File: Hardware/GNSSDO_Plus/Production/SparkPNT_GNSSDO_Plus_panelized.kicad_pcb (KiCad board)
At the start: 4 copper layers, 165.6 x 125.5 mm, 478 parts, among them J1 SMA_Edge, J10 SMA_Edge, J2 USB_C_Receptacle, J3 SMA_Edge, J4 USB_C_Receptacle, J5 MagJack_PoE, J6 microSD, J7 Qwiic_Vertical, J8 SMA_Edge, J9 Screw_Cage_3.5mm-10, Q1 MBT3904DW1, Q2 DMG2305UX, Q3 DMG2305UX, Q4 DMG2305UX, Q5 DMG2305UX, Q6 DMG2305UX, Q7 DMG2305UX, Q8 DMG2305UX, Q9 DMG2305UX, SW1 PTH_RA_h7.5mm, SW2 PTH_RA_h7.5mm, SW3 PTH_RA_h7.5mm, SW4 DPDT_Slide_SMD_7.2x3.5mm, U1 ESP32-WROVER-IE-N16R8, U10 74LVC2T45DC, U11 AP7361C-3.3V, U12 74LVC2T45DC, U13 STP3593LF, U14 74LVC2T45DC, U15 SN74LVC1G175DCK, U16 JPS-3-1+, U17 LMV7219M5, U18 MS8607-02BA, U19 PCA9306, U2 mosaic-T, U20 LMV7219M5, U23 LMV7219M5, U24 LMV7219M5, U25 AP2112K-3.3, U26 LTC4418, U27 LTC4418, U3 CH340C, U4 KSZ8041NL/I, U5 AP7361C-3.3V, U6 REC15E-2405SZ, U7 DP5305, U8 74LVC2T45DC, U9 74LVC2T45DC

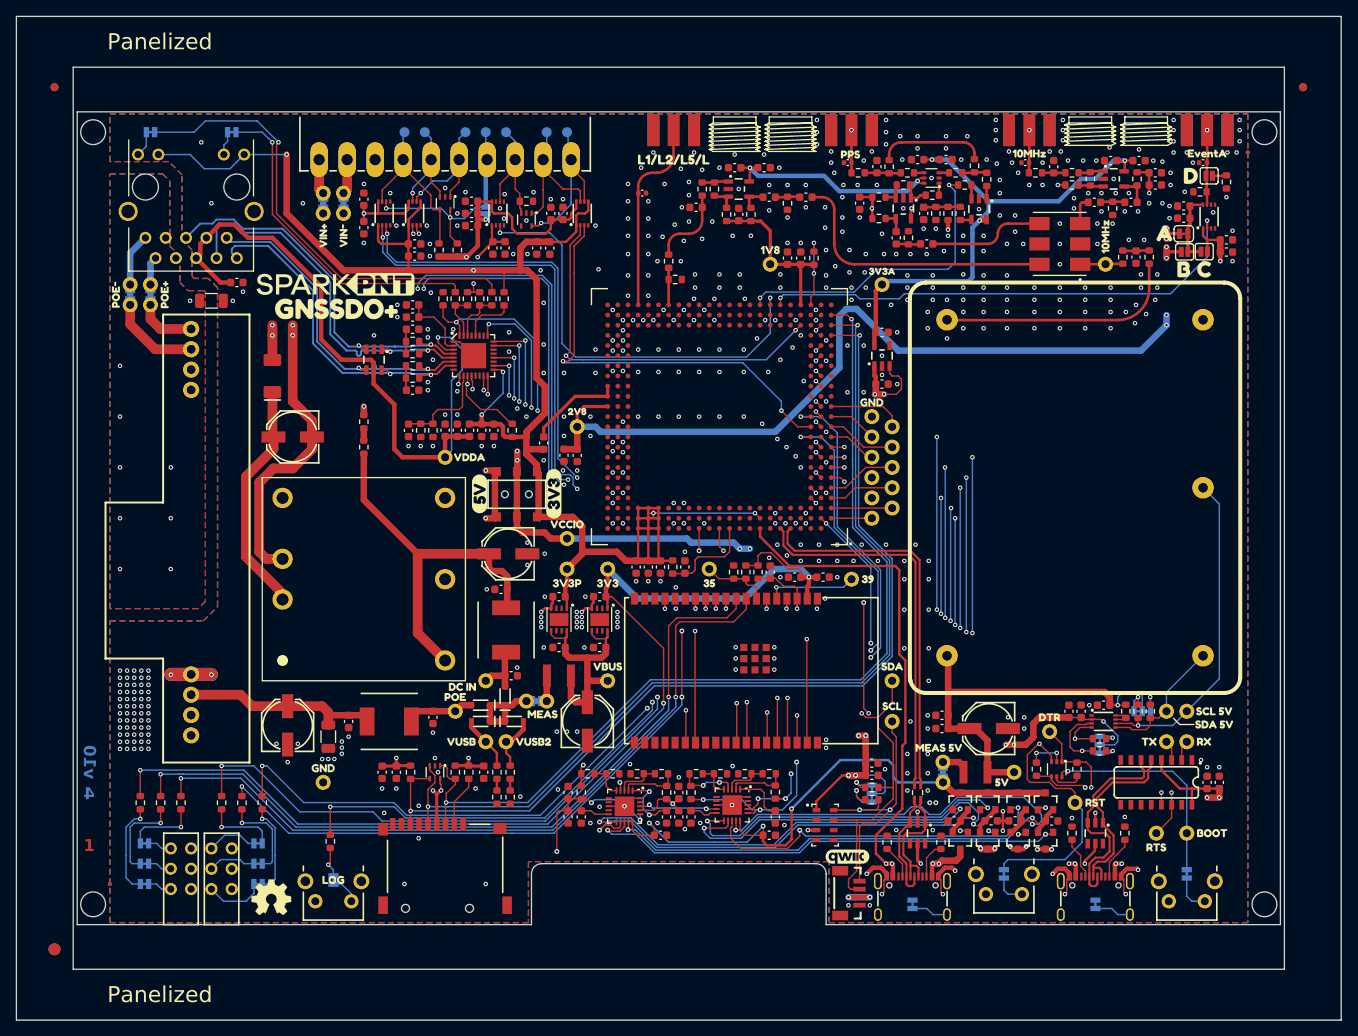
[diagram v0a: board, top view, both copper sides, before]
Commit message: KiCad 10
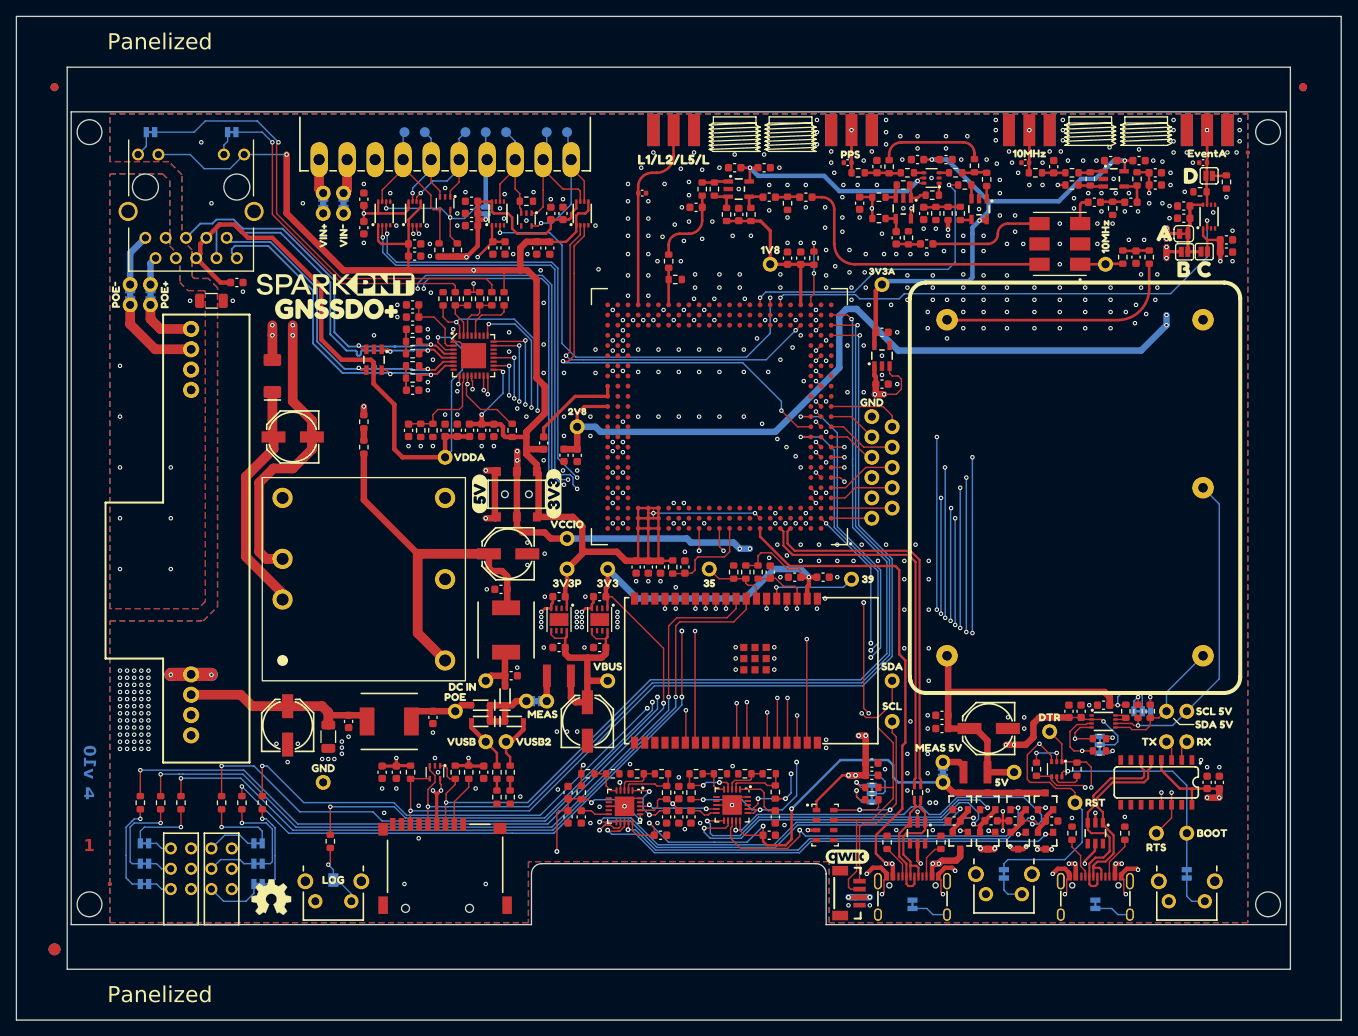
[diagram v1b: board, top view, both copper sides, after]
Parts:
- removed the ? at (99.8, 47.7) (x2)
- removed the ? at (99.8, 155.5) (x2)
- removed the ? at (255.8, 47.7) (x2)
- added ?: , Fiducial_1mm_Mask3mm, F.Cu at (255.8, 47.7)
- added ?: , Fiducial_1mm_Mask3mm, F.Cu at (99.8, 47.7)
- added ?: , Fiducial_1.5mm_Mask3mm, F.Cu at (99.8, 155.5)
- added ?: , Fiducial_1.5mm_Mask3mm, B.Cu at (99.8, 155.5)
- added ?: , Fiducial_1mm_Mask3mm, B.Cu at (99.8, 47.7)
- added ?: , Fiducial_1mm_Mask3mm, B.Cu at (255.8, 47.7)
- moved ST1 0.45 mm to (251.5, 53.3)
- moved ST3 0.45 mm to (251.5, 149.9)
- moved ST2 0.45 mm to (104.1, 53.3)
- moved ST4 0.45 mm to (104.1, 149.9)
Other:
- outline, holes or cut-outs redrawn
- board text added: "V-Score To V-Score"
